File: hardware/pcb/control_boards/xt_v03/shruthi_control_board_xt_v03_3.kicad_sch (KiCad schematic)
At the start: 50 parts, among them IC2 74HC165N, IC3 74HC165N, IC8 74595N, IC9 74HC165N, SW1 Encoder

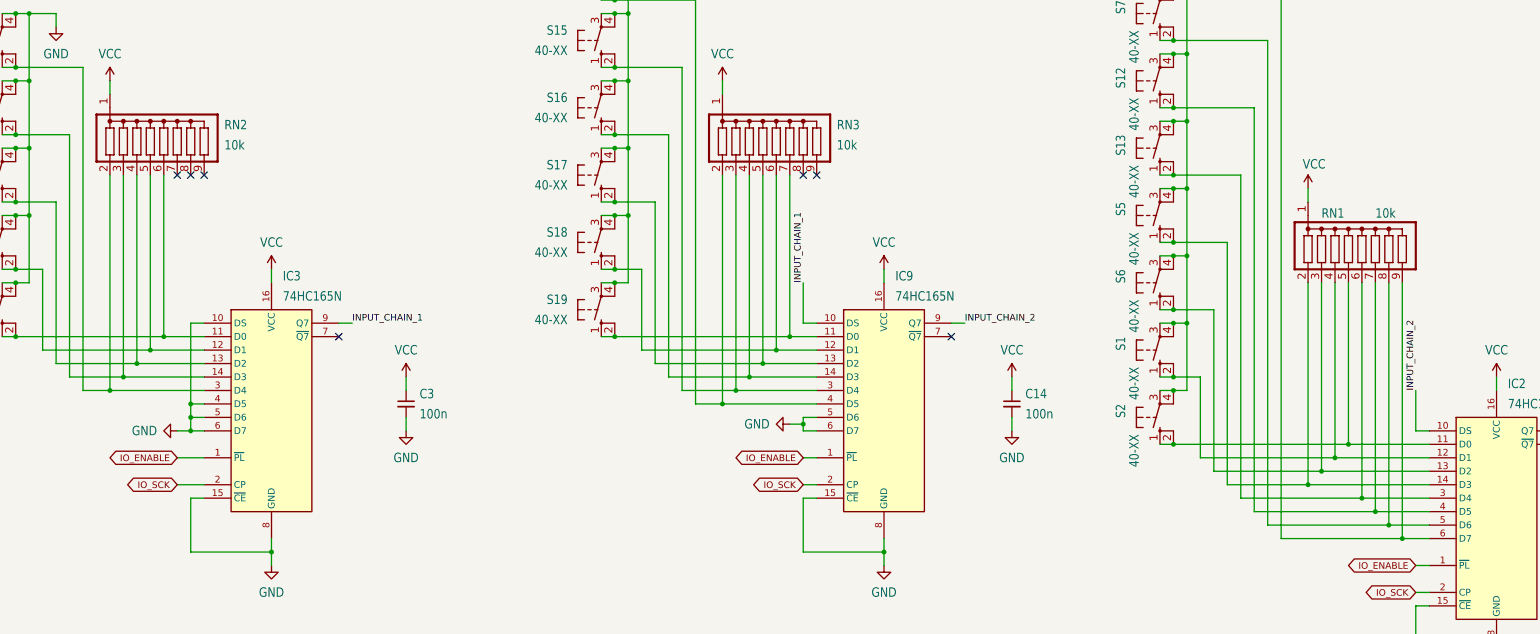
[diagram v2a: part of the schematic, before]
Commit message: update resistor networks to use kicad symbols
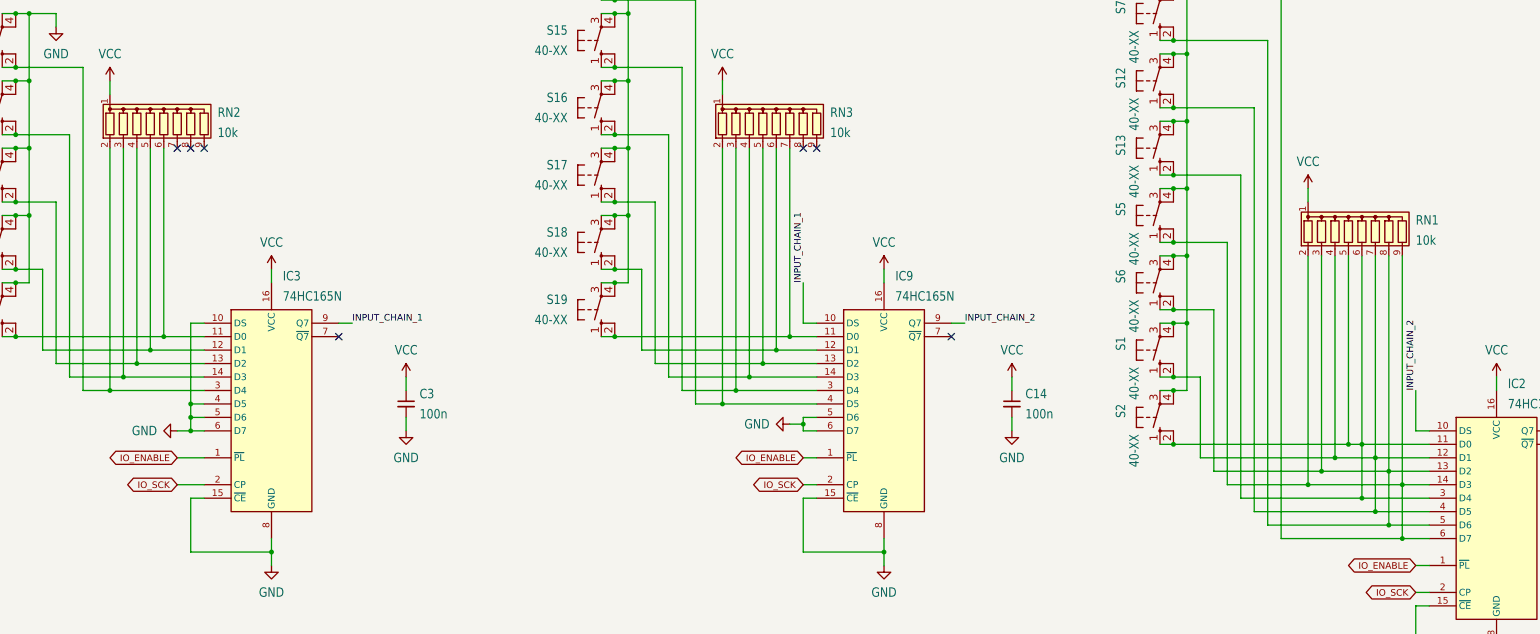
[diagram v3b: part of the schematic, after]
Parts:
- RN1, RN2, RN3: footprint shruthi_control_board_xt_v03:SIL9 -> Resistor_THT:R_Array_SIP9; symbol shruthi_control_board_xt_v03-eagle-import:G08R -> Device:R_Network08
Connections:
- net at IC2.12 (D1), RN1.4 (R3), S1.1 (S)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: now also IC2.4 (D5), RN1.7 (R6), S12.1 (S), S12.2 (S1)
- net at IC2.11 (D0), RN1.5 (R4), S2.1 (S)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: now also IC2.3 (D4), RN1.6 (R5), S13.1 (S), S13.2 (S1)
- net at IC2.6 (D7), RN1.9 (R8), S8.1 (S)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: now also IC2.14 (D3), RN1.2 (R1), S5.1 (S), S5.2 (S1)
- net at IC2.13 (D2), RN1.3 (R2), S6.1 (S)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: now also IC2.5 (D6), RN1.8 (R7), S7.1 (S), S7.2 (S1)
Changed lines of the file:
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@@
 	)
 	(junction
+		(at 347.98 137.16)
+		(diameter 0)
+		(color 0 0 0 0)
+	)
+	(junction
 		(at 204.47 66.04)
 		(diameter 0)
@@
 	)
 	(junction
+		(at 345.44 134.62)
+		(diameter 0)
+		(color 0 0 0 0)
+	)
+	(junction
 		(at 337.82 139.7)
 		(diameter 0)
@@
 	)
 	(junction
+		(at 353.06 142.24)
+		(diameter 0)
+		(color 0 0 0 0)
+	)
+	(junction
 		(at 345.44 144.78)
 		(diameter 0)
@@
 	)
 	(junction
+		(at 350.52 139.7)
+		(diameter 0)
+		(color 0 0 0 0)
+	)
+	(junction
 		(at 91.44 114.3)
 		(diameter 0)
@@
 	)
 	(no_connect
-		(at 242.57 83.82)
+		(at 242.57 78.74)
 	)
 	(no_connect
@@
 	)
 	(no_connect
-		(at 121.92 83.82)
+		(at 121.92 78.74)
 	)
 	(no_connect
@@
 	)
 	(no_connect
-		(at 127 83.82)
+		(at 127 78.74)
 	)
 	(no_connect
-		(at 124.46 83.82)
+		(at 124.46 78.74)
 	)
 	(no_connect
-		(at 240.03 83.82)
+		(at 240.03 78.74)
 	)
 	(wire
@@
 	(wire
 		(pts
-			(xy 119.38 83.82) (xy 119.38 114.3)
+			(xy 119.38 78.74) (xy 119.38 114.3)
 		)
 		(stroke
@@
 	(wire
 		(pts
-			(xy 229.87 83.82) (xy 229.87 121.92)
+			(xy 229.87 78.74) (xy 229.87 121.92)
 		)
 		(stroke
@@
 	(wire
 		(pts
-			(xy 114.3 83.82) (xy 114.3 119.38)
+			(xy 114.3 78.74) (xy 114.3 119.38)
+		)
+		(stroke
+			(width 0.1524)
+			(type solid)
+		)
+	)
+	(wire
+		(pts
+			(xy 347.98 137.16) (xy 347.98 147.32)
 		)
 		(stroke
@@
 	(wire
 		(pts
-			(xy 224.79 83.82) (xy 224.79 127)
+			(xy 224.79 78.74) (xy 224.79 127)
 		)
 		(stroke
@@
 	(wire
 		(pts
-			(xy 116.84 83.82) (xy 116.84 116.84)
+			(xy 116.84 78.74) (xy 116.84 116.84)
 		)
 		(stroke
@@
 	(wire
 		(pts
-			(xy 350.52 104.14) (xy 350.52 149.86)
+			(xy 350.52 99.06) (xy 350.52 139.7)
 		)
 		(stroke
@@
 	(wire
 		(pts
-			(xy 340.36 104.14) (xy 340.36 137.16)
+			(xy 340.36 99.06) (xy 340.36 137.16)
 		)
 		(stroke
@@
 	(wire
 		(pts
+			(xy 345.44 134.62) (xy 345.44 144.78)
+		)
+		(stroke
+			(width 0.1524)
+			(type solid)
+		)
+	)
+	(wire
+		(pts
 			(xy 124.46 127) (xy 124.46 129.54)
 		)
@@
 	(wire
 		(pts
-			(xy 111.76 83.82) (xy 111.76 121.92)
+			(xy 111.76 78.74) (xy 111.76 121.92)
+		)
+		(stroke
+			(width 0.1524)
+			(type solid)
+		)
+	)
+	(wire
+		(pts
+			(xy 350.52 139.7) (xy 350.52 149.86)
 		)
 		(stroke
@@
 	(wire
 		(pts
-			(xy 109.22 83.82) (xy 109.22 124.46)
+			(xy 109.22 78.74) (xy 109.22 124.46)
 		)
 		(stroke
@@
 	(wire
 		(pts
-			(xy 345.44 104.14) (xy 345.44 144.78)
+			(xy 345.44 99.06) (xy 345.44 134.62)
 		)
 		(stroke
@@
 	(wire
 		(pts
-			(xy 335.28 104.14) (xy 335.28 142.24)
+			(xy 335.28 99.06) (xy 335.28 142.24)
 		)
 		(stroke
@@
 	(wire
 		(pts
-			(xy 347.98 104.14) (xy 347.98 147.32)
+			(xy 347.98 99.06) (xy 347.98 137.16)
 		)
 		(stroke
@@
 	(wire
 		(pts
-			(xy 237.49 83.82) (xy 237.49 114.3)
+			(xy 237.49 78.74) (xy 237.49 114.3)
 		)
 		(stroke
@@
 	(wire
 		(pts
-			(xy 232.41 83.82) (xy 232.41 119.38)
+			(xy 232.41 78.74) (xy 232.41 119.38)
 		)
 		(stroke
@@
 	(wire
 		(pts
+			(xy 353.06 142.24) (xy 353.06 152.4)
+		)
+		(stroke
+			(width 0.1524)
+			(type solid)
+		)
+	)
+	(wire
+		(pts
 			(xy 355.6 165.1) (xy 355.6 175.26)
 		)
@@
 	(wire
 		(pts
-			(xy 234.95 83.82) (xy 234.95 116.84)
+			(xy 234.95 78.74) (xy 234.95 116.84)
 		)
 		(stroke
@@
 	(wire
 		(pts
-			(xy 353.06 104.14) (xy 353.06 152.4)
+			(xy 353.06 99.06) (xy 353.06 142.24)
 		)
 		(stroke
@@
 	(wire
 		(pts
-			(xy 337.82 104.14) (xy 337.82 139.7)
+			(xy 337.82 99.06) (xy 337.82 139.7)
 		)
 		(stroke
@@
 	(wire
 		(pts
-			(xy 227.33 124.46) (xy 227.33 83.82)
+			(xy 227.33 124.46) (xy 227.33 78.74)
 		)
 		(stroke
@@
 	(wire
 		(pts
-			(xy 342.9 104.14) (xy 342.9 134.62)
+			(xy 342.9 99.06) (xy 342.9 134.62)
 		)
 		(stroke
@@
 	)
 	(symbol
-		(lib_id "shruthi_control_board_xt_v03-eagle-import:G08R")
-		(at 119.38 78.74 0)
+		(lib_id "Device:R_Network08")
+		(at 119.38 73.66 0)
 		(unit 1)
 		(exclude_from_sim no)
@@
 		(fields_autoplaced yes)
 		(property "Reference" "RN2"
-			(at 130.81 74.3585 0)
+			(at 129.54 72.009 0)
 			(effects
 				(font
@@
 		)
 		(property "Value" "10k"
-			(at 130.81 78.1685 0)
+			(at 129.54 75.819 0)
 			(effects
 				(font
@@
 			)
 		)
-		(property "Footprint" "shruthi_control_board_xt_v03:SIL9"
-			(at 119.38 78.74 0)
+		(property "Footprint" "Resistor_THT:R_Array_SIP9"
+			(at 131.445 73.66 90)
 			(effects
 				(font
@@
 			)
 		)
-		(property "Datasheet" ""
-			(at 119.38 78.74 0)
+		(property "Datasheet" "http://www.vishay.com/docs/31509/csc.pdf"
+			(at 119.38 73.66 0)
 			(effects
 				(font
@@
 			)
 		)
-		(property "Description" ""
-			(at 119.38 78.74 0)
+		(property "Description" "8 resistor network, star topology, bussed resistors, small symbol"
+			(at 119.38 73.66 0)
 			(effects
 				(font
@@
 	)
 	(symbol
-		(lib_id "shruthi_control_board_xt_v03-eagle-import:G08R")
-		(at 345.44 99.06 0)
+		(lib_id "Device:R_Network08")
+		(at 345.44 93.98 0)
 		(unit 1)
 		(exclude_from_sim no)
@@
 		(on_board yes)
 		(dnp no)
+		(fields_autoplaced yes)
 		(property "Reference" "RN1"
-			(at 337.82 92.075 0)
+			(at 355.6 92.329 0)
 			(effects
 				(font
 					(size 1.778 1.5113)
 				)
-				(justify left bottom)
+				(justify left)
 			)
 		)
 		(property "Value" "10k"
-			(at 347.98 92.075 0)
+			(at 355.6 96.139 0)
 			(effects
 				(font
 					(size 1.778 1.5113)
 				)
-				(justify left bottom)
+				(justify left)
 			)
 		)
-		(property "Footprint" "shruthi_control_board_xt_v03:SIL9"
-			(at 345.44 99.06 0)
+		(property "Footprint" "Resistor_THT:R_Array_SIP9"
+			(at 357.505 93.98 90)
 			(effects
 				(font
@@
 			)
 		)
-		(property "Datasheet" ""
-			(at 345.44 99.06 0)
+		(property "Datasheet" "http://www.vishay.com/docs/31509/csc.pdf"
+			(at 345.44 93.98 0)
 			(effects
 				(font
@@
 			)
 		)
-		(property "Description" ""
-			(at 345.44 99.06 0)
+		(property "Description" "8 resistor network, star topology, bussed resistors, small symbol"
+			(at 345.44 93.98 0)
 			(effects
 				(font
@@
 	)
 	(symbol
-		(lib_id "shruthi_control_board_xt_v03-eagle-import:G08R")
-		(at 234.95 78.74 0)
+		(lib_id "Device:R_Network08")
+		(at 234.95 73.66 0)
 		(unit 1)
 		(exclude_from_sim no)
@@
 		(fields_autoplaced yes)
 		(property "Reference" "RN3"
-			(at 246.38 74.3585 0)
+			(at 245.11 72.009 0)
 			(effects
 				(font
@@
 		)
 		(property "Value" "10k"
-			(at 246.38 78.1685 0)
+			(at 245.11 75.819 0)
 			(effects
 				(font
@@
 			)
 		)
-		(property "Footprint" "shruthi_control_board_xt_v03:SIL9"
-			(at 234.95 78.74 0)
+		(property "Footprint" "Resistor_THT:R_Array_SIP9"
+			(at 247.015 73.66 90)
 			(effects
 				(font
@@
 			)
 		)
-		(property "Datasheet" ""
-			(at 234.95 78.74 0)
+		(property "Datasheet" "http://www.vishay.com/docs/31509/csc.pdf"
+			(at 234.95 73.66 0)
 			(effects
 				(font
@@
 			)
 		)
-		(property "Description" ""
-			(at 234.95 78.74 0)
+		(property "Description" "8 resistor network, star topology, bussed resistors, small symbol"
+			(at 234.95 73.66 0)
 			(effects
 				(font
@@
 		(on_board yes)
 		(dnp no)
+		(fields_autoplaced yes)
 		(property "Reference" "#P+20"
 			(at 335.28 86.36 0)
@@
 		)
 		(property "Value" "VCC"
-			(at 334.264 82.804 0)
+			(at 335.28 81.28 0)
 			(effects
 				(font
 					(size 1.778 1.5113)
 				)
-				(justify left bottom)
 			)
 		)

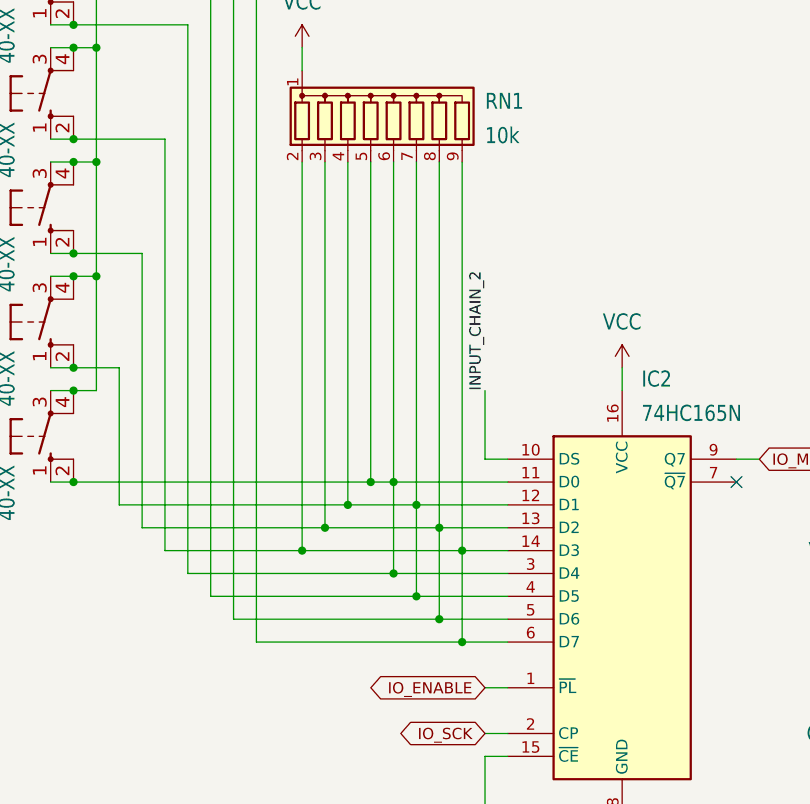
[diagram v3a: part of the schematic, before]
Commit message: fix extra connections on IC2
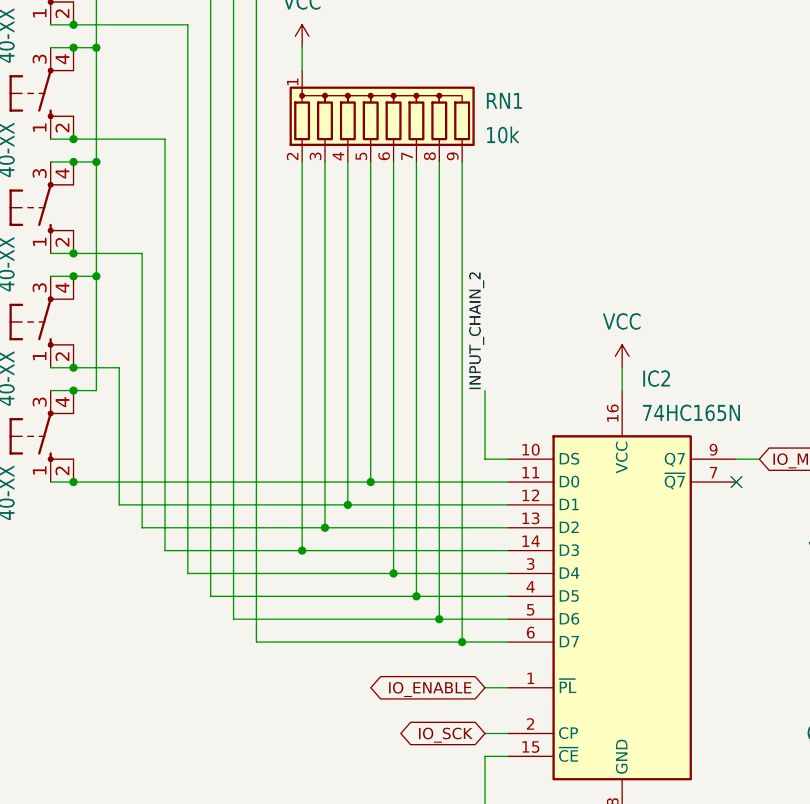
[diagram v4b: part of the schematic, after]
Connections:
- net at IC2.12 (D1), RN1.4 (R3), S1.1 (S)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: no longer IC2.4 (D5), RN1.7 (R6), S12.1 (S), S12.2 (S1)
- net at IC2.11 (D0), RN1.5 (R4), S2.1 (S)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: no longer IC2.3 (D4), RN1.6 (R5), S13.1 (S), S13.2 (S1)
- net at IC2.6 (D7), RN1.9 (R8), S8.1 (S)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: no longer IC2.14 (D3), RN1.2 (R1), S5.1 (S), S5.2 (S1)
- net at IC2.13 (D2), RN1.3 (R2), S6.1 (S)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: no longer IC2.5 (D6), RN1.8 (R7), S7.1 (S), S7.2 (S1)
- new net: IC2.14 (D3), RN1.2 (R1), S5.1 (S), S5.2 (S1)
- new net: IC2.3 (D4), RN1.6 (R5), S13.1 (S), S13.2 (S1)
- new net: IC2.4 (D5), RN1.7 (R6), S12.1 (S), S12.2 (S1)
- new net: IC2.5 (D6), RN1.8 (R7), S7.1 (S), S7.2 (S1)
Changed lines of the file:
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@@
-	)
-	(junction
-		(at 347.98 137.16)
-		(diameter 0)
-		(color 0 0 0 0)
 	)
 	(junction
@@
 	)
 	(junction
-		(at 345.44 134.62)
-		(diameter 0)
-		(color 0 0 0 0)
-	)
-	(junction
 		(at 337.82 139.7)
 		(diameter 0)
@@
 	)
 	(junction
-		(at 353.06 142.24)
-		(diameter 0)
-		(color 0 0 0 0)
-	)
-	(junction
 		(at 345.44 144.78)
 		(diameter 0)
@@
 	(junction
 		(at 91.44 88.9)
-		(diameter 0)
-		(color 0 0 0 0)
-	)
-	(junction
-		(at 350.52 139.7)
 		(diameter 0)
 		(color 0 0 0 0)
@@
 	(wire
 		(pts
-			(xy 353.06 142.24) (xy 358.14 142.24)
+			(xy 335.28 142.24) (xy 358.14 142.24)
 		)
 		(stroke
@@
 	(wire
 		(pts
-			(xy 345.44 134.62) (xy 358.14 134.62)
-		)
-		(stroke
-			(width 0.1524)
-			(type solid)
-		)
-	)
-	(wire
-		(pts
 			(xy 165.1 218.44) (xy 167.64 218.44)
 		)
@@
 	(wire
 		(pts
-			(xy 337.82 139.7) (xy 350.52 139.7)
-		)
-		(stroke
-			(width 0.1524)
-			(type solid)
-		)
-	)
-	(wire
-		(pts
 			(xy 55.88 236.22) (xy 55.88 233.68)
 		)
@@
 	(wire
 		(pts
-			(xy 347.98 137.16) (xy 347.98 147.32)
-		)
-		(stroke
-			(width 0.1524)
-			(type solid)
-		)
-	)
-	(wire
-		(pts
 			(xy 34.29 77.47) (xy 36.83 77.47)
 		)
@@
 	(wire
 		(pts
-			(xy 342.9 134.62) (xy 345.44 134.62)
+			(xy 342.9 134.62) (xy 358.14 134.62)
 		)
 		(stroke
@@
 	(wire
 		(pts
-			(xy 350.52 99.06) (xy 350.52 139.7)
-		)
-		(stroke
-			(width 0.1524)
-			(type solid)
-		)
-	)
-	(wire
-		(pts
 			(xy 127 142.24) (xy 121.92 142.24)
 		)
@@
 	(wire
 		(pts
-			(xy 345.44 134.62) (xy 345.44 144.78)
-		)
-		(stroke
-			(width 0.1524)
-			(type solid)
-		)
-	)
-	(wire
-		(pts
 			(xy 124.46 127) (xy 124.46 129.54)
 		)
@@
 	(wire
 		(pts
-			(xy 350.52 139.7) (xy 350.52 149.86)
+			(xy 350.52 99.06) (xy 350.52 149.86)
 		)
 		(stroke
@@
 	(wire
 		(pts
-			(xy 350.52 139.7) (xy 358.14 139.7)
+			(xy 337.82 139.7) (xy 358.14 139.7)
 		)
 		(stroke
@@
 	(wire
 		(pts
-			(xy 347.98 137.16) (xy 358.14 137.16)
-		)
-		(stroke
-			(width 0.1524)
-			(type solid)
-		)
-	)
-	(wire
-		(pts
 			(xy 134.62 228.6) (xy 129.54 228.6)
 		)
@@
 	(wire
 		(pts
-			(xy 345.44 99.06) (xy 345.44 134.62)
+			(xy 345.44 99.06) (xy 345.44 144.78)
 		)
 		(stroke
@@
 	(wire
 		(pts
-			(xy 347.98 99.06) (xy 347.98 137.16)
+			(xy 347.98 99.06) (xy 347.98 147.32)
 		)
 		(stroke
@@
 	(wire
 		(pts
-			(xy 340.36 137.16) (xy 347.98 137.16)
+			(xy 340.36 137.16) (xy 358.14 137.16)
 		)
 		(stroke
@@
 	(wire
 		(pts
-			(xy 353.06 142.24) (xy 353.06 152.4)
+			(xy 353.06 99.06) (xy 353.06 152.4)
 		)
 		(stroke
@@
 	(wire
 		(pts
-			(xy 335.28 142.24) (xy 353.06 142.24)
-		)
-		(stroke
-			(width 0.1524)
-			(type solid)
-		)
-	)
-	(wire
-		(pts
 			(xy 139.7 218.44) (xy 156.21 218.44)
 		)
@@
 		)
 		(stroke
-			(width 0.1524)
-			(type solid)
-		)
-	)
-	(wire
-		(pts
-			(xy 353.06 99.06) (xy 353.06 142.24)
-		)
-		(stroke
